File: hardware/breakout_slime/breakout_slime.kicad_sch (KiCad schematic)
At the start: 11 parts, among them J1 IMU_Conn_Female, SW1 SW_SPST, U1 TP4056_Break, U2 WeMos_D1_mini, U3 BNO/MPU_Break

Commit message: Assigned Footprints
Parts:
- J1: footprint (none) -> Connector_PinSocket_2.54mm:PinSocket_1x05_P2.54mm_Horizontal
- JP1, JP2: footprint (none) -> Jumper:SolderJumper-2_P1.3mm_Open_Pad1.0x1.5mm
- R1: footprint (none) -> Resistor_THT:R_Axial_DIN0207_L6.3mm_D2.5mm_P10.16mm_Horizontal
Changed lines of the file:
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@@
     (property "Reference" "R1" (id 0) (at 148.59 36.068 90))
     (property "Value" "180K" (id 1) (at 148.59 38.1 90))
-    (property "Footprint" "" (id 2) (at 148.59 39.878 90)
+    (property "Footprint" "Resistor_THT:R_Axial_DIN0207_L6.3mm_D2.5mm_P10.16mm_Horizontal" (id 2) (at 148.59 39.878 90)
       (effects (font (size 1.27 1.27)) hide)
     )
@@
       (effects (font (size 1.27 1.27)) (justify left))
     )
-    (property "Footprint" "" (id 2) (at 184.15 34.29 0)
+    (property "Footprint" "Connector_PinSocket_2.54mm:PinSocket_1x05_P2.54mm_Horizontal" (id 2) (at 184.15 34.29 0)
       (effects (font (size 1.27 1.27)) hide)
     )
@@
     (property "Reference" "JP1" (id 0) (at 172.72 73.152 0))
     (property "Value" "AD0_BNO_JP" (id 1) (at 172.72 68.58 0))
-    (property "Footprint" "" (id 2) (at 172.72 71.12 0)
+    (property "Footprint" "Jumper:SolderJumper-2_P1.3mm_Open_Pad1.0x1.5mm" (id 2) (at 172.72 71.12 0)
       (effects (font (size 1.27 1.27)) hide)
     )
@@
     (property "Reference" "JP2" (id 0) (at 184.912 83.82 0))
     (property "Value" "AD0_MPU_JP" (id 1) (at 180.34 83.82 0))
-    (property "Footprint" "" (id 2) (at 182.88 83.82 0)
+    (property "Footprint" "Jumper:SolderJumper-2_P1.3mm_Open_Pad1.0x1.5mm" (id 2) (at 182.88 83.82 0)
       (effects (font (size 1.27 1.27)) hide)
     )
@@
     )
     (path "/8230d6de-8acf-4bbc-8fef-ea7a4839a964"
-      (reference "J1") (unit 1) (value "IMU_Conn_Female") (footprint "")
+      (reference "J1") (unit 1) (value "IMU_Conn_Female") (footprint "Connector_PinSocket_2.54mm:PinSocket_1x05_P2.54mm_Horizontal")
     )
     (path "/9d0913ab-8eb9-4882-8aab-3c1d167bd626"
-      (reference "JP1") (unit 1) (value "AD0_BNO_JP") (footprint "")
+      (reference "JP1") (unit 1) (value "AD0_BNO_JP") (footprint "Jumper:SolderJumper-2_P1.3mm_Open_Pad1.0x1.5mm")
     )
     (path "/e3d56755-9723-4ec6-bf71-df45693dba3e"
-      (reference "JP2") (unit 1) (value "AD0_MPU_JP") (footprint "")
+      (reference "JP2") (unit 1) (value "AD0_MPU_JP") (footprint "Jumper:SolderJumper-2_P1.3mm_Open_Pad1.0x1.5mm")
     )
     (path "/153f41b0-5a04-48a5-b9df-33540a5c9c00"
-      (reference "R1") (unit 1) (value "180K") (footprint "")
+      (reference "R1") (unit 1) (value "180K") (footprint "Resistor_THT:R_Axial_DIN0207_L6.3mm_D2.5mm_P10.16mm_Horizontal")
     )
     (path "/f354bada-f44b-41e7-bb08-dbf978916cbe"

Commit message: Added TP4056 breakout and assigned more footprints
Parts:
- BT1: footprint (none) -> Connector_JST:JST_PH_S2B-PH-K_1x02_P2.00mm_Horizontal
- SW1: footprint (none) -> Button_Switch_THT:SW_CuK_OS102011MA1QN1_SPDT_Angled
- U1: footprint (none) -> slimevr_pcb:TP4056_Breakout
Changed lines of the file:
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@@
     (property "Reference" "U1" (id 0) (at 40.64 45.72 0))
     (property "Value" "TP4056_Break" (id 1) (at 57.15 45.72 0))
-    (property "Footprint" "" (id 2) (at 52.07 57.15 0)
+    (property "Footprint" "slimevr_pcb:TP4056_Breakout" (id 2) (at 52.07 57.15 0)
       (effects (font (size 1.27 1.27)) hide)
     )
@@
       (effects (font (size 1.27 1.27)) (justify left))
     )
-    (property "Footprint" "" (id 2) (at 73.66 56.896 90)
+    (property "Footprint" "Connector_JST:JST_PH_S2B-PH-K_1x02_P2.00mm_Horizontal" (id 2) (at 73.66 56.896 90)
       (effects (font (size 1.27 1.27)) hide)
     )
@@
     (property "Reference" "SW1" (id 0) (at 64.135 74.93 0))
     (property "Value" "SW_SPST" (id 1) (at 69.85 74.93 0))
-    (property "Footprint" "" (id 2) (at 67.31 74.93 0)
+    (property "Footprint" "Button_Switch_THT:SW_CuK_OS102011MA1QN1_SPDT_Angled" (id 2) (at 67.31 74.93 0)
       (effects (font (size 1.27 1.27)) hide)
     )
@@
     )
     (path "/45a250e1-9915-4fdf-8e3c-ba6bb77fd179"
-      (reference "BT1") (unit 1) (value "Battery_Cell") (footprint "")
+      (reference "BT1") (unit 1) (value "Battery_Cell") (footprint "Connector_JST:JST_PH_S2B-PH-K_1x02_P2.00mm_Horizontal")
     )
     (path "/ed8fc088-b5df-4712-9ff0-f28aba923a95"
@@
     )
     (path "/f354bada-f44b-41e7-bb08-dbf978916cbe"
-      (reference "SW1") (unit 1) (value "SW_SPST") (footprint "")
+      (reference "SW1") (unit 1) (value "SW_SPST") (footprint "Button_Switch_THT:SW_CuK_OS102011MA1QN1_SPDT_Angled")
     )
     (path "/199a8760-de9f-4640-8d96-efab787d1919"
-      (reference "U1") (unit 1) (value "TP4056_Break") (footprint "")
+      (reference "U1") (unit 1) (value "TP4056_Break") (footprint "slimevr_pcb:TP4056_Breakout")
     )
     (path "/842cd130-03dc-45ef-b1ee-5e8df8a8b56c"

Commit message: Added BNO_MPU_Breakout
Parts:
- U3: footprint (none) -> slimevr_pcb:BNO_MPU_Breakout
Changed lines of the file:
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@@
     (property "Reference" "U3" (id 0) (at 203.2 59.69 0))
     (property "Value" "BNO/MPU_Break" (id 1) (at 203.2 77.47 0))
-    (property "Footprint" "" (id 2) (at 194.31 72.39 0)
+    (property "Footprint" "slimevr_pcb:BNO_MPU_Breakout" (id 2) (at 194.31 72.39 0)
       (effects (font (size 1.27 1.27)) hide)
     )
@@
     )
     (path "/2d6d9858-3970-4237-b9d0-a8ee11d9dc9f"
-      (reference "U3") (unit 1) (value "BNO/MPU_Break") (footprint "")
-    )
-  )
+      (reference "U3") (unit 1) (value "BNO/MPU_Break") (footprint "slimevr_pcb:BNO_MPU_Breakout")
+    )
+  )

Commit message: Finished board rev 0.1
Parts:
- J1: footprint Connector_PinSocket_2.54mm:PinSocket_1x05_P2.54mm_Horizontal -> Connector_JST:JST_PH_S5B-PH-K_1x05_P2.00mm_Horizontal
- SW1: value SW_SPST -> SW_SPDT; symbol Switch:SW_SPST -> Switch:SW_SPDT
- U1: value TP4056_Break -> TP4056_Breakout; symbol slimevr_pcb:TP4056_Break -> slimevr_pcb:TP4056_Breakout
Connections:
- net +3V3: now also U3.1 (VCC); no longer U3. (VCC)
- net GND: now also SW1.2 (B), U3.2 (GND); no longer SW1.1 (A), U3. (VCC)
- net INT1: now also U3.6 (INT/AD0_MPU); no longer U3. (VCC)
- net SCL: now also U3.3 (SCL); no longer U3. (VCC)
- net SDA: now also U3.4 (SDA); no longer U3. (VCC)
- net at U1.3 (Out-): now also SW1.3 (C); no longer SW1.2 (B)
- net at JP1.1 (A): now also U3.5 (AD0_BNO); no longer U3. (VCC)
- no-connect marks 9 -> 10
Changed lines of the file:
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@@
   (title_block
     (title "breakout_slime")
-    (date "2022-02-23")
+    (date "2022-02-27")
     (rev "0.1")
     (company "https://github.com/TheButlah/slimevr_pcb")
@@
   )
   (no_connect (at 143.51 40.64))
+  (no_connect (at 64.77 69.85))
   (no_connect (at 123.19 50.8))
   (no_connect (at 123.19 48.26))
@@
     (stroke (width 0) (type default) (color 0 0 0 0))
   )
+  (wire (pts (xy 69.85 64.77) (xy 67.31 64.77))
+    (stroke (width 0) (type default) (color 0 0 0 0))
+  )
   (polyline (pts (xy 208.28 13.97) (xy 161.29 13.97))
     (stroke (width 0) (type default) (color 0 0 0 0))
@@
     (stroke (width 0) (type default) (color 0 0 0 0))
   )
-  (wire (pts (xy 67.31 64.77) (xy 67.31 69.85))
-    (stroke (width 0) (type default) (color 0 0 0 0))
-  )
   (wire (pts (xy 67.31 81.28) (xy 67.31 83.82))
     (stroke (width 0) (type default) (color 0 0 0 0))
@@
   )
   (wire (pts (xy 73.66 48.26) (xy 73.66 53.34))
+    (stroke (width 0) (type default) (color 0 0 0 0))
+  )
+  (wire (pts (xy 69.85 69.85) (xy 69.85 64.77))
     (stroke (width 0) (type default) (color 0 0 0 0))
   )
@@
     (pin "2")
   )
-  (symbol (lib_id "slimevr_pcb:TP4056_Break") (at 52.07 57.15 0) (unit 1)
+  (symbol (lib_id "slimevr_pcb:TP4056_Breakout") (at 52.07 57.15 0) (unit 1)
     (in_bom yes) (on_board yes)
     (property "Reference" "U1" (id 0) (at 40.64 45.72 0))
-    (property "Value" "TP4056_Break" (id 1) (at 57.15 45.72 0))
+    (property "Value" "TP4056_Breakout" (id 1) (at 57.15 45.72 0))
     (property "Footprint" "slimevr_pcb:TP4056_Breakout" (id 2) (at 52.07 57.15 0)
       (effects (font (size 1.27 1.27)) hide)
@@
       (effects (font (size 1.27 1.27)) hide)
     )
-    (pin "")
-    (pin "")
-    (pin "")
-    (pin "")
-    (pin "")
-    (pin "")
+    (pin "1")
+    (pin "2")
+    (pin "3")
+    (pin "4")
+    (pin "5")
+    (pin "6")
   )
   (symbol (lib_id "power:GND") (at 67.31 83.82 0) (unit 1)
@@
       (effects (font (size 1.27 1.27)) (justify left))
     )
-    (property "Footprint" "Connector_PinSocket_2.54mm:PinSocket_1x05_P2.54mm_Horizontal" (id 2) (at 184.15 34.29 0)
+    (property "Footprint" "Connector_JST:JST_PH_S5B-PH-K_1x05_P2.00mm_Horizontal" (id 2) (at 184.15 34.29 0)
       (effects (font (size 1.27 1.27)) hide)
     )
@@
     (pin "2")
   )
-  (symbol (lib_id "Switch:SW_SPST") (at 67.31 74.93 90) (unit 1)
-    (in_bom yes) (on_board yes) (fields_autoplaced)
-    (property "Reference" "SW1" (id 0) (at 64.135 74.93 0))
-    (property "Value" "SW_SPST" (id 1) (at 69.85 74.93 0))
+  (symbol (lib_id "Switch:SW_SPDT") (at 67.31 74.93 90) (unit 1)
+    (in_bom yes) (on_board yes) (fields_autoplaced)
+    (property "Reference" "SW1" (id 0) (at 62.992 74.93 0))
+    (property "Value" "SW_SPDT" (id 1) (at 72.39 74.93 0))
     (property "Footprint" "Button_Switch_THT:SW_CuK_OS102011MA1QN1_SPDT_Angled" (id 2) (at 67.31 74.93 0)
       (effects (font (size 1.27 1.27)) hide)
@@
     (pin "1")
     (pin "2")
+    (pin "3")
   )
   (symbol (lib_id "power:+3V3") (at 182.88 55.88 0) (unit 1)
@@
     )
     (path "/8230d6de-8acf-4bbc-8fef-ea7a4839a964"
-      (reference "J1") (unit 1) (value "IMU_Conn_Female") (footprint "Connector_PinSocket_2.54mm:PinSocket_1x05_P2.54mm_Horizontal")
+      (reference "J1") (unit 1) (value "IMU_Conn_Female") (footprint "Connector_JST:JST_PH_S5B-PH-K_1x05_P2.00mm_Horizontal")
     )
     (path "/9d0913ab-8eb9-4882-8aab-3c1d167bd626"
@@
     )
     (path "/f354bada-f44b-41e7-bb08-dbf978916cbe"
-      (reference "SW1") (unit 1) (value "SW_SPST") (footprint "Button_Switch_THT:SW_CuK_OS102011MA1QN1_SPDT_Angled")
+      (reference "SW1") (unit 1) (value "SW_SPDT") (footprint "Button_Switch_THT:SW_CuK_OS102011MA1QN1_SPDT_Angled")
     )
     (path "/199a8760-de9f-4640-8d96-efab787d1919"
-      (reference "U1") (unit 1) (value "TP4056_Break") (footprint "slimevr_pcb:TP4056_Breakout")
+      (reference "U1") (unit 1) (value "TP4056_Breakout") (footprint "slimevr_pcb:TP4056_Breakout")
     )
     (path "/842cd130-03dc-45ef-b1ee-5e8df8a8b56c"

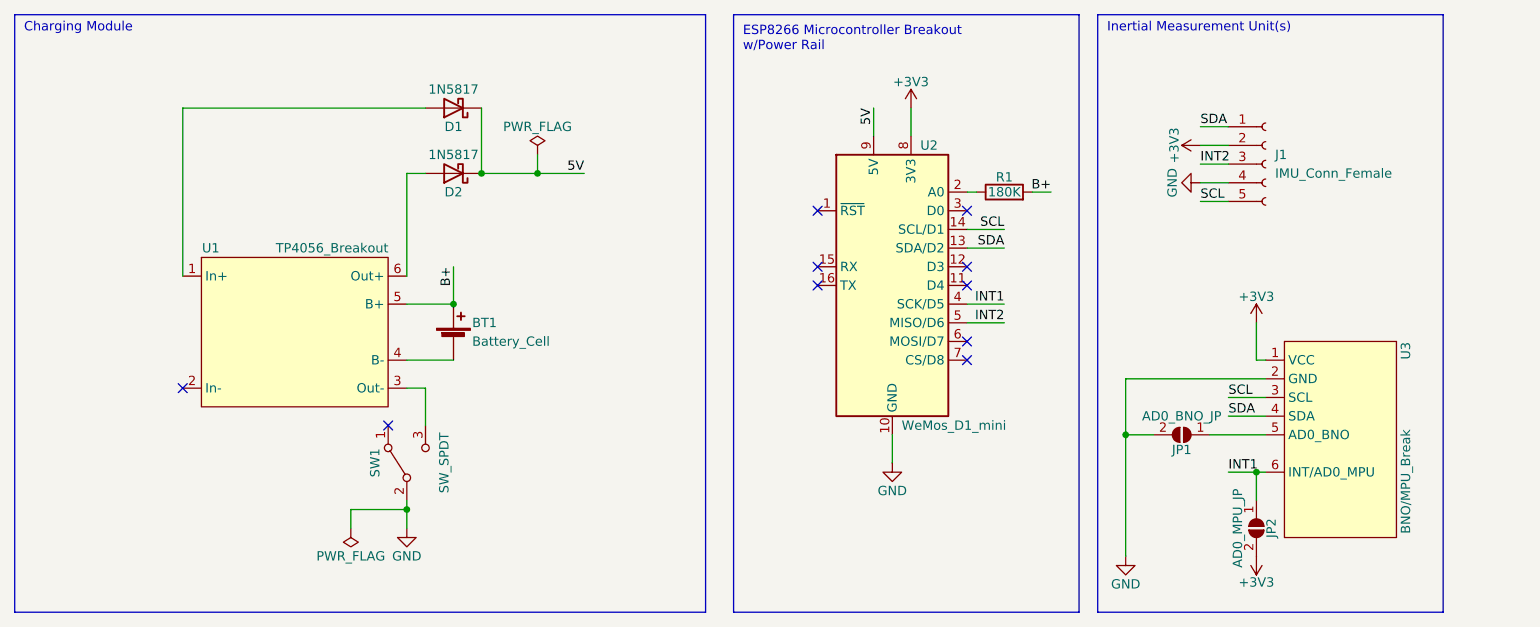
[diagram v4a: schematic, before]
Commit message: Fixed battery connector polarity on breakout_slime
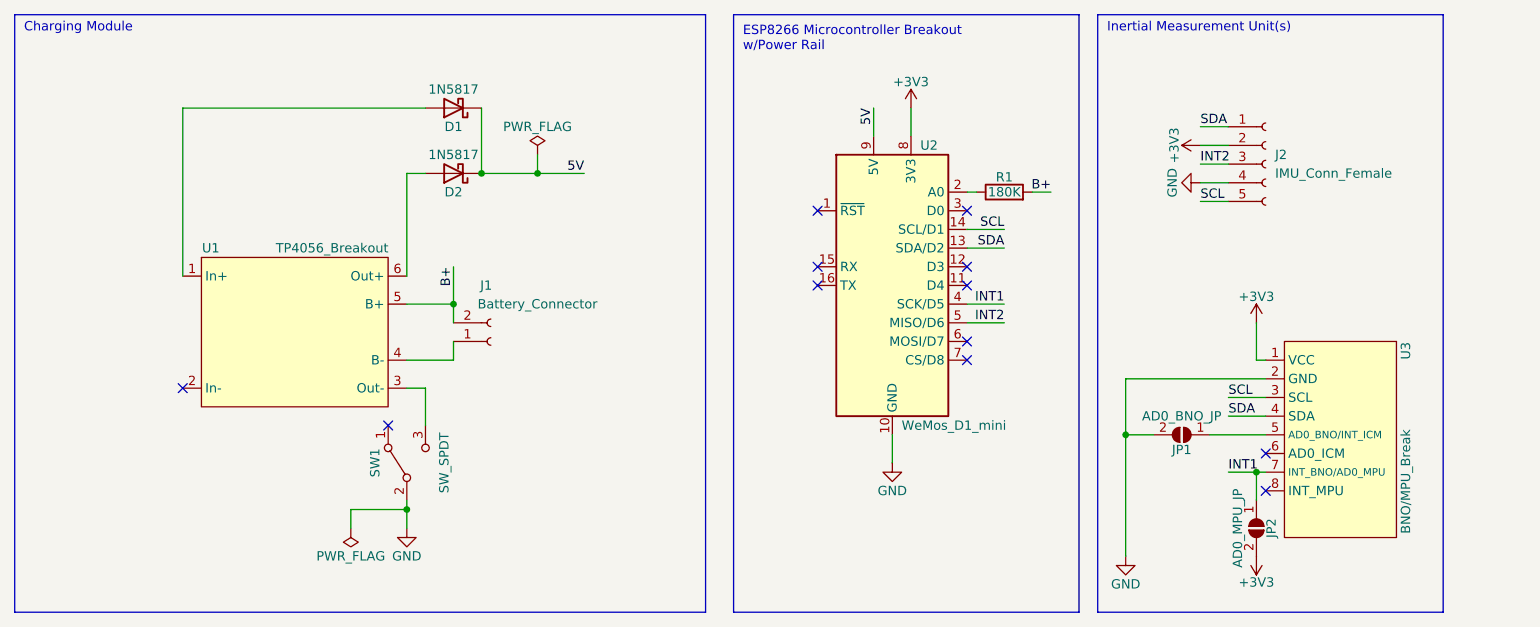
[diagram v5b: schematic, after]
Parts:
- removed BT1: Battery_Cell, Connector_JST:JST_PH_S2B-PH-K_1x02_P2.00mm_Horizontal, symbol Device:Battery_Cell
- added J1: Battery_Connector, Connector_JST:JST_PH_S2B-PH-K_1x02_P2.00mm_Horizontal, symbol Connector:Conn_01x02_Female
- U3: footprint slimevr_pcb:BNO_MPU_Breakout -> slimevr_pcb:BNO_MPU_ICM_Breakout; symbol slimevr_pcb:BNO/MPU_Break -> slimevr_pcb:BNO/MPU/ICM_Break
- renumbered J1 to J2
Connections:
- net B+: now also J1.2 (Pin_2)
- net INT1: now also U3.7 (INT_BNO/AD0_MPU); no longer U3.6 (INT/AD0_MPU)
- net at U1.4 (B-): now also J1.1 (Pin_1)
- no-connect marks 10 -> 12
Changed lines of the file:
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@@
   (junction (at 182.88 76.2) (diameter 0) (color 0 0 0 0)
   )
+  (junction (at 165.1 71.12) (diameter 0) (color 0 0 0 0)
+  )
   (junction (at 73.66 53.34) (diameter 0) (color 0 0 0 0)
   )
-  (junction (at 165.1 71.12) (diameter 0) (color 0 0 0 0)
-  )
   (junction (at 85.09 35.56) (diameter 0) (color 0 0 0 0)
   )
@@
   (junction (at 77.47 35.56) (diameter 0) (color 0 0 0 0)
   )
+  (no_connect (at 184.15 73.66))
+  (no_connect (at 184.15 78.74))
   (no_connect (at 143.51 40.64))
   (no_connect (at 64.77 69.85))
@@
     (stroke (width 0) (type default) (color 0 0 0 0))
   )
+  (wire (pts (xy 73.66 53.34) (xy 73.66 55.88))
+    (stroke (width 0) (type default) (color 0 0 0 0))
+  )
   (polyline (pts (xy 13.97 13.97) (xy 13.97 95.25))
+    (stroke (width 0) (type default) (color 0 0 0 0))
+  )
+  (wire (pts (xy 73.66 58.42) (xy 73.66 60.96))
     (stroke (width 0) (type default) (color 0 0 0 0))
   )
@@
     (pin "1")
   )
-  (symbol (lib_id "slimevr_pcb:BNO{slash}MPU_Break") (at 194.31 72.39 270) (unit 1)
+  (symbol (lib_id "slimevr_pcb:BNO{slash}MPU{slash}ICM_Break") (at 194.31 72.39 270) (unit 1)
     (in_bom yes) (on_board yes) (fields_autoplaced)
     (property "Reference" "U3" (id 0) (at 203.2 59.69 0))
     (property "Value" "BNO/MPU_Break" (id 1) (at 203.2 77.47 0))
-    (property "Footprint" "slimevr_pcb:BNO_MPU_Breakout" (id 2) (at 194.31 72.39 0)
+    (property "Footprint" "slimevr_pcb:BNO_MPU_ICM_Breakout" (id 2) (at 207.01 71.12 0)
       (effects (font (size 1.27 1.27)) hide)
     )
@@
     (pin "5")
     (pin "6")
+    (pin "7")
+    (pin "8")
   )
   (symbol (lib_id "power:GND") (at 67.31 83.82 0) (unit 1)
@@
     (pin "1")
   )
-  (symbol (lib_id "Device:Battery_Cell") (at 73.66 58.42 0) (unit 1)
-    (in_bom yes) (on_board yes) (fields_autoplaced)
-    (property "Reference" "BT1" (id 0) (at 76.2 55.88 0)
-      (effects (font (size 1.27 1.27)) (justify left))
-    )
-    (property "Value" "Battery_Cell" (id 1) (at 76.2 58.42 0)
-      (effects (font (size 1.27 1.27)) (justify left))
-    )
-    (property "Footprint" "Connector_JST:JST_PH_S2B-PH-K_1x02_P2.00mm_Horizontal" (id 2) (at 73.66 56.896 90)
-      (effects (font (size 1.27 1.27)) hide)
-    )
-    (property "Datasheet" "~" (id 3) (at 73.66 56.896 90)
-      (effects (font (size 1.27 1.27)) hide)
-    )
-    (pin "1")
-    (pin "2")
-  )
   (symbol (lib_id "power:PWR_FLAG") (at 85.09 33.02 0) (unit 1)
     (in_bom yes) (on_board yes) (fields_autoplaced)
@@
   (symbol (lib_id "Connector:Conn_01x05_Female") (at 184.15 34.29 0) (unit 1)
     (in_bom yes) (on_board yes) (fields_autoplaced)
-    (property "Reference" "J1" (id 0) (at 185.42 33.0199 0)
+    (property "Reference" "J2" (id 0) (at 185.42 33.0199 0)
       (effects (font (size 1.27 1.27)) (justify left))
     )
@@
     (pin "2")
   )
+  (symbol (lib_id "Connector:Conn_01x02_Female") (at 78.74 58.42 0) (mirror x) (unit 1)
+    (in_bom yes) (on_board yes)
+    (property "Reference" "J1" (id 0) (at 78.105 50.8 0))
+    (property "Value" "Battery_Connector" (id 1) (at 85.09 53.34 0))
+    (property "Footprint" "Connector_JST:JST_PH_S2B-PH-K_1x02_P2.00mm_Horizontal" (id 2) (at 78.74 58.42 0)
+      (effects (font (size 1.27 1.27)) hide)
+    )
+    (property "Datasheet" "~" (id 3) (at 78.74 58.42 0)
+      (effects (font (size 1.27 1.27)) hide)
+    )
+    (pin "1")
+    (pin "2")
+  )
   (symbol (lib_id "power:+3V3") (at 182.88 87.63 180) (unit 1)
     (in_bom yes) (on_board yes) (fields_autoplaced)
@@
       (reference "#PWR08") (unit 1) (value "+3V3") (footprint "")
     )
-    (path "/45a250e1-9915-4fdf-8e3c-ba6bb77fd179"
-      (reference "BT1") (unit 1) (value "Battery_Cell") (footprint "Connector_JST:JST_PH_S2B-PH-K_1x02_P2.00mm_Horizontal")
-    )
     (path "/ed8fc088-b5df-4712-9ff0-f28aba923a95"
       (reference "D1") (unit 1) (value "1N5817") (footprint "Diode_THT:D_DO-41_SOD81_P10.16mm_Horizontal")
@@
       (reference "D2") (unit 1) (value "1N5817") (footprint "Diode_THT:D_DO-41_SOD81_P10.16mm_Horizontal")
     )
+    (path "/b4b3542d-81a0-443a-a057-e92e83e673be"
+      (reference "J1") (unit 1) (value "Battery_Connector") (footprint "Connector_JST:JST_PH_S2B-PH-K_1x02_P2.00mm_Horizontal")
+    )
     (path "/8230d6de-8acf-4bbc-8fef-ea7a4839a964"
-      (reference "J1") (unit 1) (value "IMU_Conn_Female") (footprint "Connector_JST:JST_PH_S5B-PH-K_1x05_P2.00mm_Horizontal")
+      (reference "J2") (unit 1) (value "IMU_Conn_Female") (footprint "Connector_JST:JST_PH_S5B-PH-K_1x05_P2.00mm_Horizontal")
     )
     (path "/9d0913ab-8eb9-4882-8aab-3c1d167bd626"
@@
     )
     (path "/2d6d9858-3970-4237-b9d0-a8ee11d9dc9f"
-      (reference "U3") (unit 1) (value "BNO/MPU_Break") (footprint "slimevr_pcb:BNO_MPU_Breakout")
-    )
-  )
+      (reference "U3") (unit 1) (value "BNO/MPU_Break") (footprint "slimevr_pcb:BNO_MPU_ICM_Breakout")
+    )
+  )

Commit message: breakout_slime v0.1.2
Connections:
- net 5V renamed +5V
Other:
- moved on the sheet: U3
